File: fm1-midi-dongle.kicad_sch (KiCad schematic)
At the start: 28 parts, among them J1 USB-C plug to FM-1, J2 USB-C power in, J3 MIDI OUT TRS, J4 MIDI IN TRS, J5 SDI (WCH-LinkE), U1 CH32X035G8U6, U2 XC6206P332MR, U3 SY6280AAC, U4 H11L1SM

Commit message: Schematic: LCSC# field on every component; passives verified on lcsc.com
Co-Authored-By: Claude Fable 5.1 <noreply@anthropic.com>
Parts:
- C1, C2, C3: LCSC# (none) -> C15849
- C4, C5: LCSC# (none) -> C14663
- D1: LCSC# (none) -> C81598
- D2: LCSC# (none) -> C72043
- J1: LCSC C3151751 -> (none); LCSC# (none) -> C3151751
- J2: LCSC C165948 -> (none); LCSC# (none) -> C165948
- J3, J4: LCSC C18594 -> (none); LCSC# (none) -> C18594
- J5: LCSC# (none) -> C2337
- R1: LCSC# (none) -> C23206
- R10: LCSC# (none) -> C25804
- R11: LCSC# (none) -> C21190
- R12: LCSC# (none) -> C25803
- R2, R3: LCSC# (none) -> C23186
- R4: LCSC# (none) -> C23212
- R5, R6: LCSC# (none) -> C22809
- R7: LCSC# (none) -> C22859
- R8: LCSC# (none) -> C23140
- R9: LCSC# (none) -> C22962
- U1: LCSC C7437027 -> (none); LCSC# (none) -> C7437027
- U2: LCSC C5446 -> (none); LCSC# (none) -> C5446
- U3: LCSC C55136 -> (none); LCSC# (none) -> C55136
- U4: LCSC C899473 -> (none); LCSC# (none) -> C899473

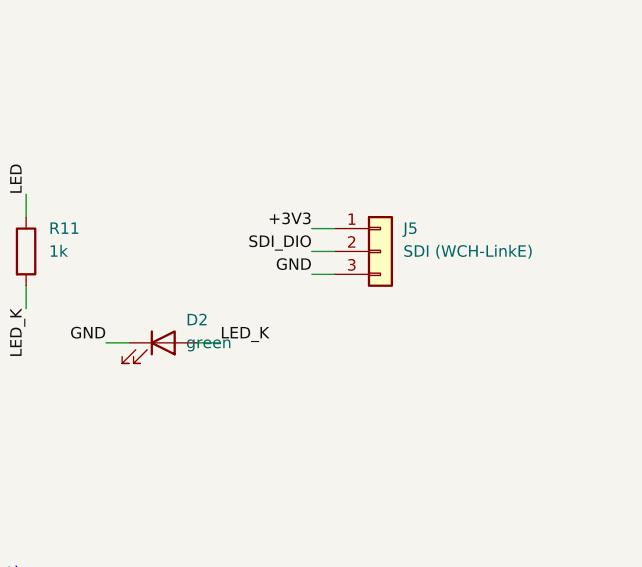
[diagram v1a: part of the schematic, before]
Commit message: Replace the SDI pin header with three bare pads; nothing bulky on the stick
Co-Authored-By: Claude Fable 5.1 <noreply@anthropic.com>
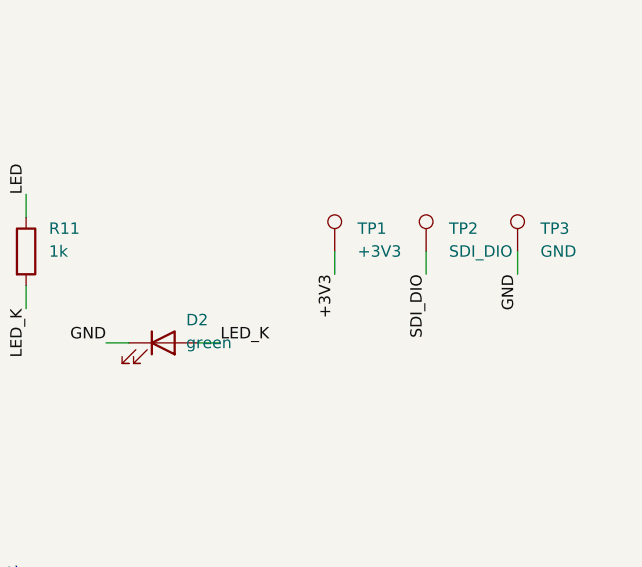
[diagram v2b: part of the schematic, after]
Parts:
- removed J5: SDI (WCH-LinkE), Connector_PinHeader_2.54mm:PinHeader_1x03_P2.54mm_Vertical, symbol Connector_Generic:Conn_01x03
- added TP1: +3V3, TestPoint:TestPoint_Pad_1.5x1.5mm, symbol Connector:TestPoint
- added TP2: SDI_DIO, TestPoint:TestPoint_Pad_1.5x1.5mm, symbol Connector:TestPoint
- added TP3: GND, TestPoint:TestPoint_Pad_1.5x1.5mm, symbol Connector:TestPoint
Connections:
- net +3V3: now also TP1.1
- net GND: now also TP3.1
- net SDI_DIO: now also TP2.1
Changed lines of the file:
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@@
 	(wire (pts (xy 269.24 160.02) (xy 271.78 160.02)) (stroke (width 0) (type default)))
 	(label "LED_K" (at 271.78 160.02 0) (effects (font (size 1.27 1.27)) (justify left bottom)))
-	(symbol (lib_id "Connector_Generic:Conn_01x03") (at 289.56 149.86 0) (unit 1) (exclude_from_sim no) (in_bom yes) (on_board yes) (dnp no)
-		(property "Reference" "J5" (at 292.1 147.32 0) (effects (font (size 1.27 1.27)) (justify left)))
-		(property "Value" "SDI (WCH-LinkE)" (at 292.1 149.86 0) (effects (font (size 1.27 1.27)) (justify left)))
-		(property "Footprint" "Connector_PinHeader_2.54mm:PinHeader_1x03_P2.54mm_Vertical" (at 289.56 149.86 0) (effects (font (size 1.27 1.27)) (justify left) (hide yes)))
-		(property "Datasheet" "~" (at 289.56 149.86 0) (effects (font (size 1.27 1.27)) (justify left) (hide yes)))
-		(property "LCSC#" "C2337" (at 289.56 149.86 0) (effects (font (size 1.27 1.27)) (justify left) (hide yes)))
-		(property "Note" "3V3 / DIO (PC18, pin 25) / GND" (at 289.56 149.86 0) (effects (font (size 1.27 1.27)) (justify left) (hide yes)))
+	(symbol (lib_id "Connector:TestPoint") (at 284.48 149.86 0) (unit 1) (exclude_from_sim no) (in_bom yes) (on_board yes) (dnp no)
+		(property "Reference" "TP1" (at 287.02 147.32 0) (effects (font (size 1.27 1.27)) (justify left)))
+		(property "Value" "+3V3" (at 287.02 149.86 0) (effects (font (size 1.27 1.27)) (justify left)))
+		(property "Footprint" "TestPoint:TestPoint_Pad_1.5x1.5mm" (at 284.48 149.86 0) (effects (font (size 1.27 1.27)) (justify left) (hide yes)))
+		(property "Datasheet" "~" (at 284.48 149.86 0) (effects (font (size 1.27 1.27)) (justify left) (hide yes)))
+		(property "Note" "SDI pad: 3V3 / DIO (PC18, pin 25) / GND" (at 284.48 149.86 0) (effects (font (size 1.27 1.27)) (justify left) (hide yes)))
 		(pin "1")
-		(pin "2")
-		(pin "3")
-		(instances (project "fm1-midi-dongle" (path "/7f2a1c4e-0b3d-4c1a-9e8f-5a6b7c8d9e0f" (reference "J5") (unit 1))))
+		(instances (project "fm1-midi-dongle" (path "/7f2a1c4e-0b3d-4c1a-9e8f-5a6b7c8d9e0f" (reference "TP1") (unit 1))))
 	)
-	(wire (pts (xy 284.48 147.32) (xy 281.94 147.32)) (stroke (width 0) (type default)))
-	(label "+3V3" (at 281.94 147.32 180) (effects (font (size 1.27 1.27)) (justify right bottom)))
-	(wire (pts (xy 284.48 149.86) (xy 281.94 149.86)) (stroke (width 0) (type default)))
-	(label "SDI_DIO" (at 281.94 149.86 180) (effects (font (size 1.27 1.27)) (justify right bottom)))
-	(wire (pts (xy 284.48 152.4) (xy 281.94 152.4)) (stroke (width 0) (type default)))
-	(label "GND" (at 281.94 152.4 180) (effects (font (size 1.27 1.27)) (justify right bottom)))
+	(wire (pts (xy 284.48 149.86) (xy 284.48 152.4)) (stroke (width 0) (type default)))
+	(label "+3V3" (at 284.48 152.4 270) (effects (font (size 1.27 1.27)) (justify right bottom)))
+	(symbol (lib_id "Connector:TestPoint") (at 294.64 149.86 0) (unit 1) (exclude_from_sim no) (in_bom yes) (on_board yes) (dnp no)
+		(property "Reference" "TP2" (at 297.18 147.32 0) (effects (font (size 1.27 1.27)) (justify left)))
+		(property "Value" "SDI_DIO" (at 297.18 149.86 0) (effects (font (size 1.27 1.27)) (justify left)))
+		(property "Footprint" "TestPoint:TestPoint_Pad_1.5x1.5mm" (at 294.64 149.86 0) (effects (font (size 1.27 1.27)) (justify left) (hide yes)))
+		(property "Datasheet" "~" (at 294.64 149.86 0) (effects (font (size 1.27 1.27)) (justify left) (hide yes)))
+		(property "Note" "SDI pad: 3V3 / DIO (PC18, pin 25) / GND" (at 294.64 149.86 0) (effects (font (size 1.27 1.27)) (justify left) (hide yes)))
+		(pin "1")
+		(instances (project "fm1-midi-dongle" (path "/7f2a1c4e-0b3d-4c1a-9e8f-5a6b7c8d9e0f" (reference "TP2") (unit 1))))
+	)
+	(wire (pts (xy 294.64 149.86) (xy 294.64 152.4)) (stroke (width 0) (type default)))
+	(label "SDI_DIO" (at 294.64 152.4 270) (effects (font (size 1.27 1.27)) (justify right bottom)))
+	(symbol (lib_id "Connector:TestPoint") (at 304.8 149.86 0) (unit 1) (exclude_from_sim no) (in_bom yes) (on_board yes) (dnp no)
+		(property "Reference" "TP3" (at 307.34 147.32 0) (effects (font (size 1.27 1.27)) (justify left)))
+		(property "Value" "GND" (at 307.34 149.86 0) (effects (font (size 1.27 1.27)) (justify left)))
+		(property "Footprint" "TestPoint:TestPoint_Pad_1.5x1.5mm" (at 304.8 149.86 0) (effects (font (size 1.27 1.27)) (justify left) (hide yes)))
+		(property "Datasheet" "~" (at 304.8 149.86 0) (effects (font (size 1.27 1.27)) (justify left) (hide yes)))
+		(property "Note" "SDI pad: 3V3 / DIO (PC18, pin 25) / GND" (at 304.8 149.86 0) (effects (font (size 1.27 1.27)) (justify left) (hide yes)))
+		(pin "1")
+		(instances (project "fm1-midi-dongle" (path "/7f2a1c4e-0b3d-4c1a-9e8f-5a6b7c8d9e0f" (reference "TP3") (unit 1))))
+	)
+	(wire (pts (xy 304.8 149.86) (xy 304.8 152.4)) (stroke (width 0) (type default)))
+	(label "GND" (at 304.8 152.4 270) (effects (font (size 1.27 1.27)) (justify right bottom)))
 	(symbol (lib_id "power:+5V") (at 39.37 190.5 0) (unit 1) (exclude_from_sim no) (in_bom yes) (on_board yes) (dnp no)
 		(property "Reference" "#PWR01" (at 41.91 187.96 0) (effects (font (size 1.27 1.27)) (justify left)))

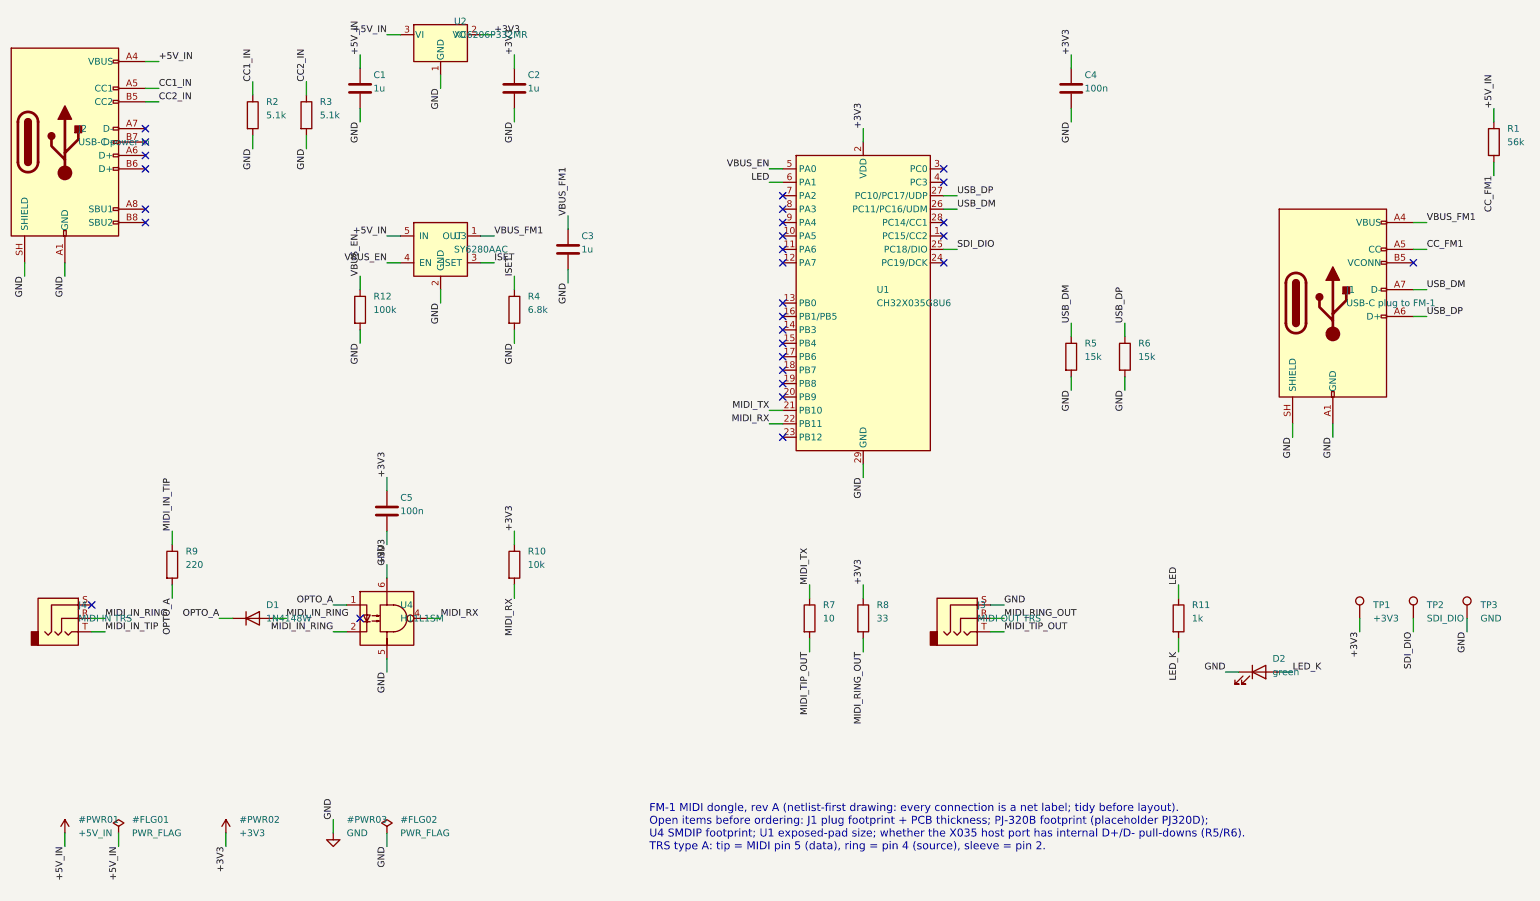
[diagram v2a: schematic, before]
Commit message: Design for JLCPCB assembly: exact LCSC footprints from EasyEDA, PJ-320D jacks, 0.8 mm board for the edge-clamp plug, JLCPCB BOM export
- footprints + 3D models for every IC and connector pulled with easyeda2kicad for the exact LCSC numbers
- USB-C plug datasheet read: PCB 0.80 +/-0.05 mm, pads on both faces; JLCPCB Standard assembly only
- PJ-320B dropped (EasyEDA entry is a dummy 'not a PCB-soldered part'); PJ-320D C521460 with pin map
  verified against KiCad's named PJ320D footprint (1 sleeve, 2 ring2, 3 ring1, 4 tip)
- values are manufacturer part numbers so the JLCPCB Comment column is right; test pads out of the BOM
- tools/export_jlc.sh -> production/bom_jlcpcb.csv

Co-Authored-By: Claude Fable 5.1 <noreply@anthropic.com>
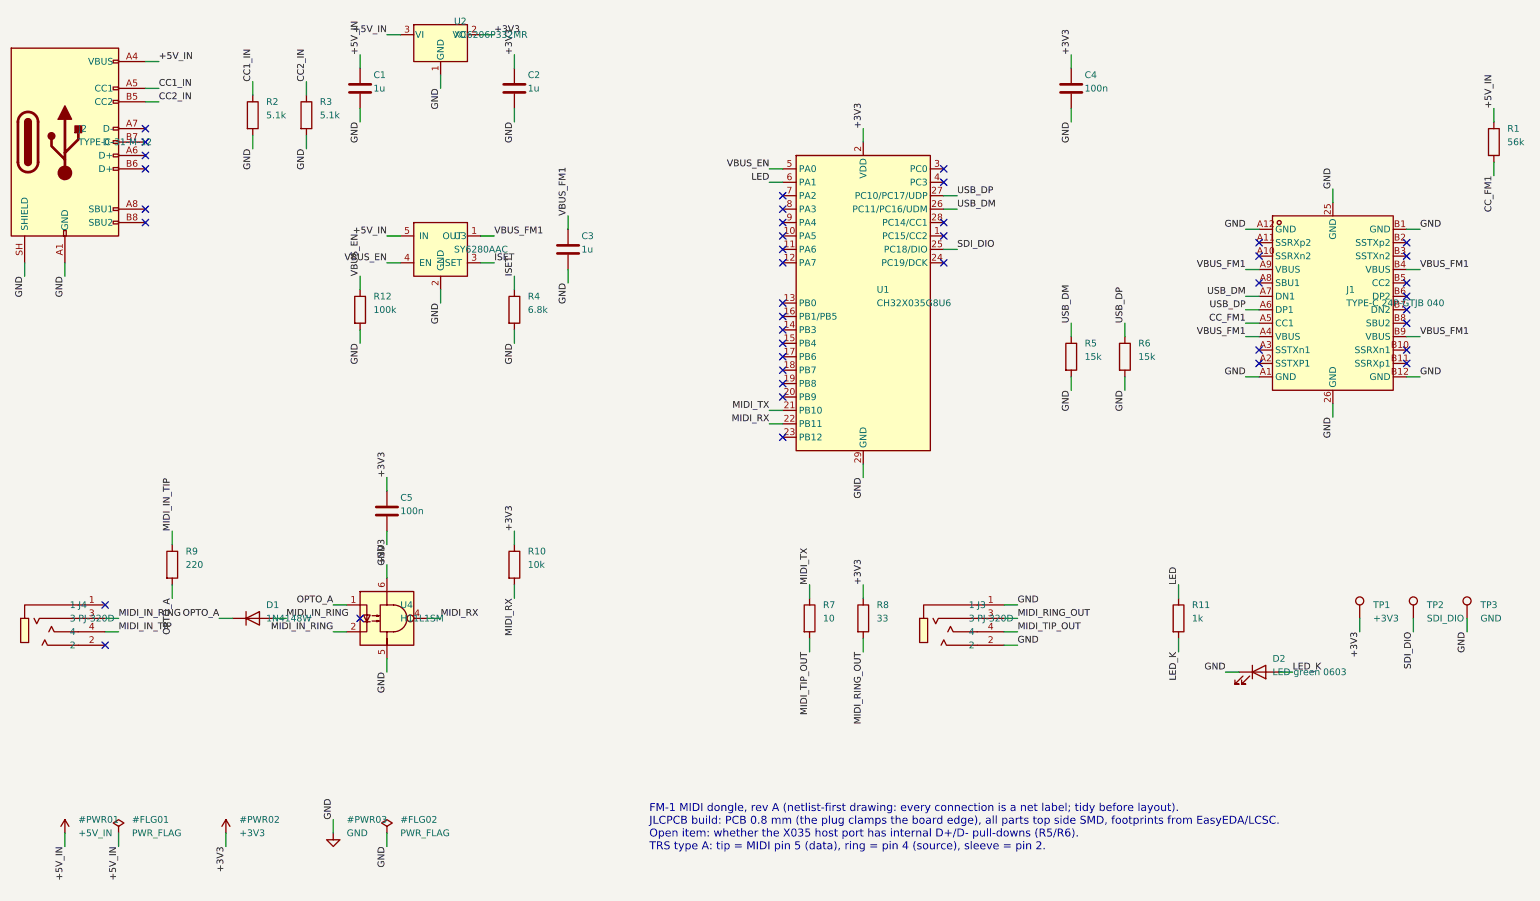
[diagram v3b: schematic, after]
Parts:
- removed J1: USB-C plug to FM-1, symbol Connector:USB_C_Plug_USB2.0
- removed J3: MIDI OUT TRS, Connector_Audio:Jack_3.5mm_PJ320D_Horizontal, symbol Connector_Audio:AudioJack3
- removed J4: MIDI IN TRS, Connector_Audio:Jack_3.5mm_PJ320D_Horizontal, symbol Connector_Audio:AudioJack3
- added J1: TYPE-C 24P-GTJB 040, fm1_dongle:USB-C-SMD_TYPE-C-24P-GTJB-040, symbol fm1_dongle:USB-C_Plug_GTJB040
- added J3, J4: PJ-320D, fm1_dongle:AUDIO-SMD_PJ-320D, symbol fm1_dongle:PJ-320D
- D2: value green -> LED green 0603
- J2: value USB-C power in -> TYPE-C-31-M-12
- TP1, TP2, TP3: now left out of the parts list
- U1: footprint Package_DFN_QFN:WQFN-28-1EP_4x4mm_P0.4mm_EP2.7x2.7mm -> fm1_dongle:QFN-28_L4.0-W4.0-P0.40-BL-EP2.8; Note QFN28 F7P6/TSSOP20 has NO USB host; G8U6 required. footprint = KiCad symbol default; EP size not in the datasheet text, verify on the drawing. -> QFN28 F7P6/TSSOP20 has NO USB host; G8U6 required. footprint from EasyEDA/LCSC for C7437027 (EP 2.8 mm).
- U2: footprint Package_TO_SOT_SMD:SOT-23-3 -> fm1_dongle:SOT-23-3_L2.9-W1.6-P1.90-LS2.8-BR
- U3: footprint Package_TO_SOT_SMD:SOT-23-5 -> fm1_dongle:SOT-23-5_L3.0-W1.7-P0.95-LS2.8-BL
- U4: footprint Package_DIP:SMDIP-6_W7.62mm -> fm1_dongle:SOP-6_L8.5-W6.4-P2.54-LS9.2-BL; Note SMD gull-wing 6-pin; footprint to verify against onsemi dra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 -> footprint from EasyEDA/LCSC for C899473
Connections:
- net CC_FM1: now also J1.A5 (CC1)
- net GND: now also J1.25 (GND), J1.26 (GND), J1.A1 (GND), J1.A12 (GND), J1.B1 (GND), J1.B12 (GND), J3.1, J3.2
- net MIDI_IN_RING: now also J4.3
- net MIDI_IN_TIP: now also J4.4
- net MIDI_RING_OUT: now also J3.3
- net MIDI_TIP_OUT: now also J3.4
- net USB_DM: now also J1.A7 (DN1)
- net USB_DP: now also J1.A6 (DP1)
- net VBUS_FM1: now also J1.A4 (VBUS), J1.A9 (VBUS), J1.B4 (VBUS), J1.B9 (VBUS)
- no-connect marks 29 -> 42
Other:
- note added: "FM-1 MIDI dongle, rev A (netlist-first drawing: every connection is a net label; tidy before layout). JLCPCB build: PCB 0.8 mm (the plug clamps the board edge), all parts top side SMD, footprints from EasyEDA/LCSC. Open item: whether the X035 host port has internal D+/D- pull-downs (R5/R6). TRS type A: tip = MIDI pin 5 (data), ring = pin 4 (source), sleeve = pin 2."
- note removed: "FM-1 MIDI dongle, rev A (netlist-first drawing: every connection is a net label; tidy before layout). Open items before ordering: J1 plug footprint + PCB thickness; PJ-320B footprint (placeholder PJ320D); U4 SMDIP footprint; U1 exposed-pad size; whether the X035 host port has internal D+/D- pull-downs (R5/R6). TRS type A: tip = MIDI pin 5 (data), ring = pin 4 (source), sleeve = pin 2."

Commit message: PCB floorplan: 18.9 x 26 mm, 4 layers, 0.8 mm, generated from the netlist with pcbnew
- plug tongue edge with latch notches drawn exactly from the plug drawing; housing off-board
- jacks at 9.3 mm pitch on the far edge, receptacle on the bottom right, opto bottom left,
  MCU top right in the hole-free band, passives in columns under the jacks
- JLCPCB 4-layer rules, GND plane on In1, keep-out under the plug clamp; DRC clean except silk
- R5/R6 DNP (X035 host port has internal pull-downs); deterministic schematic uuids so the
  PCB stays linked across regenerations

Co-Authored-By: Claude Fable 5.1 <noreply@anthropic.com>
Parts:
- R5: Note host-side pull-down; drop if the X035 host port has interna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 -> DNP: the X035 host port has internal pull-downs (RB_UH_PD_D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; now not fitted
- R6: now not fitted
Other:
- note added: "FM-1 MIDI dongle, rev A (netlist-first drawing: every connection is a net label; tidy before layout). JLCPCB build: PCB 0.8 mm (the plug clamps the board edge), all parts top side SMD, footprints from EasyEDA/LCSC. R5/R6 are DNP: the X035 host port has internal D+/D- pull-downs (RB_UH_PD_DIS = 0). TRS type A: tip = MIDI pin 5 (data), ring = pin 4 (source), sleeve = pin 2."
- note removed: "FM-1 MIDI dongle, rev A (netlist-first drawing: every connection is a net label; tidy before layout). JLCPCB build: PCB 0.8 mm (the plug clamps the board edge), all parts top side SMD, footprints from EasyEDA/LCSC. Open item: whether the X035 host port has internal D+/D- pull-downs (R5/R6). TRS type A: tip = MIDI pin 5 (data), ring = pin 4 (source), sleeve = pin 2."
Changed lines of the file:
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@@
 	(wire (pts (xy 229.87 53.34) (xy 229.87 55.88)) (stroke (width 0) (type default)))
 	(label "GND" (at 229.87 55.88 270) (effects (font (size 1.27 1.27)) (justify right bottom)))
-	(symbol (lib_id "Device:R") (at 229.87 100.33 0) (unit 1) (exclude_from_sim no) (in_bom yes) (on_board yes) (dnp no)
+	(symbol (lib_id "Device:R") (at 229.87 100.33 0) (unit 1) (exclude_from_sim no) (in_bom yes) (on_board yes) (dnp yes)
 		(property "Reference" "R5" (at 232.41 97.79 0) (effects (font (size 1.27 1.27)) (justify left)))
 		(property "Value" "15k" (at 232.41 100.33 0) (effects (font (size 1.27 1.27)) (justify left)))
@@
 		(property "Datasheet" "~" (at 229.87 100.33 0) (effects (font (size 1.27 1.27)) (justify left) (hide yes)))
 		(property "LCSC#" "C22809" (at 229.87 100.33 0) (effects (font (size 1.27 1.27)) (justify left) (hide yes)))
-		(property "Note" "host-side pull-down; drop if the X035 host port has internal ones (RM check)" (at 229.87 100.33 0) (effects (font (size 1.27 1.27)) (justify left) (hide yes)))
+		(property "Note" "DNP: the X035 host port has internal pull-downs (RB_UH_PD_DIS = 0, RM USBFS host chapter)" (at 229.87 100.33 0) (effects (font (size 1.27 1.27)) (justify left) (hide yes)))
 		(pin "1")
 		(pin "2")
@@
 	(wire (pts (xy 229.87 104.14) (xy 229.87 106.68)) (stroke (width 0) (type default)))
 	(label "GND" (at 229.87 106.68 270) (effects (font (size 1.27 1.27)) (justify right bottom)))
-	(symbol (lib_id "Device:R") (at 240.03 100.33 0) (unit 1) (exclude_from_sim no) (in_bom yes) (on_board yes) (dnp no)
+	(symbol (lib_id "Device:R") (at 240.03 100.33 0) (unit 1) (exclude_from_sim no) (in_bom yes) (on_board yes) (dnp yes)
 		(property "Reference" "R6" (at 242.57 97.79 0) (effects (font (size 1.27 1.27)) (justify left)))
 		(property "Value" "15k" (at 242.57 100.33 0) (effects (font (size 1.27 1.27)) (justify left)))
@@
 	(wire (pts (xy 100.33 190.5) (xy 100.33 193.04)) (stroke (width 0) (type default)))
 	(label "GND" (at 100.33 193.04 270) (effects (font (size 1.27 1.27)) (justify right bottom)))
-	(text "FM-1 MIDI dongle, rev A (netlist-first drawing: every connection is a net label; tidy before layout).\nJLCPCB build: PCB 0.8 mm (the plug clamps the board edge), all parts top side SMD, footprints from EasyEDA/LCSC.\nOpen item: whether the X035 host port has internal D+/D- pull-downs (R5/R6).\nTRS type A: tip = MIDI pin 5 (data), ring = pin 4 (source), sleeve = pin 2." (exclude_from_sim no) (at 150 185 0) (effects (font (size 1.5 1.5)) (justify left top)))
+	(text "FM-1 MIDI dongle, rev A (netlist-first drawing: every connection is a net label; tidy before layout).\nJLCPCB build: PCB 0.8 mm (the plug clamps the board edge), all parts top side SMD, footprints from EasyEDA/LCSC.\nR5/R6 are DNP: the X035 host port has internal D+/D- pull-downs (RB_UH_PD_DIS = 0).\nTRS type A: tip = MIDI pin 5 (data), ring = pin 4 (source), sleeve = pin 2." (exclude_from_sim no) (at 150 185 0) (effects (font (size 1.5 1.5)) (justify left top)))
 	(sheet_instances (path "/" (page "1")))
 	(embedded_fonts no)
